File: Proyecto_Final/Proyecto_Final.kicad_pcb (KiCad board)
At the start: 2 copper layers, 68.6 x 53.3 mm, 98 parts, among them J1 Conn_01x10, J10 Conn_01x02, J2 Conn_01x08, J3 USB_OTG, J4 Conn_01x08, J5 Conn_01x06, J6 Conn_01x02, J7 Conn_01x02, J8 Conn_02x03_Odd_Even, J9 Conn_02x03_Odd_Even, Q1 MMBT3904, Q2 MMBT3904, Q3 MMBT3904, Q4 MMBT3904, Q5 MMBT3904, Q6 MMBT3904, SW1 SW_Push, SW2 SW_Push, SW3 SW_Push, SW4 SW_Push, SW5 SW_Push, SW6 SW_Push, U1 TPS61087DSCR, U2 LM1117-3.3, U3 L293D, U4 FT232RL, U5 ATXMEGA32A4U-AU, U6 MODULE-BLUETOOTH-HC-05(34P-27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

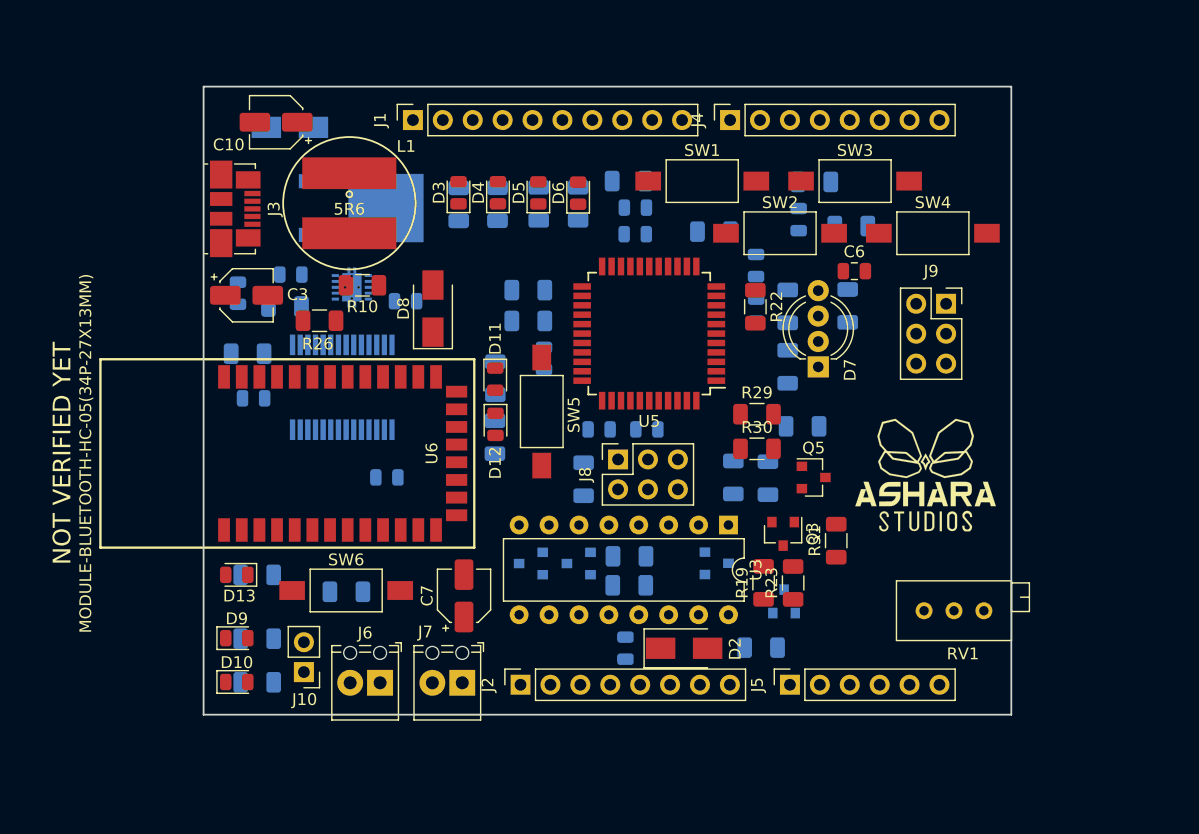
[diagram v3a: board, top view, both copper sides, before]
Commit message: se crean zonas de tierra
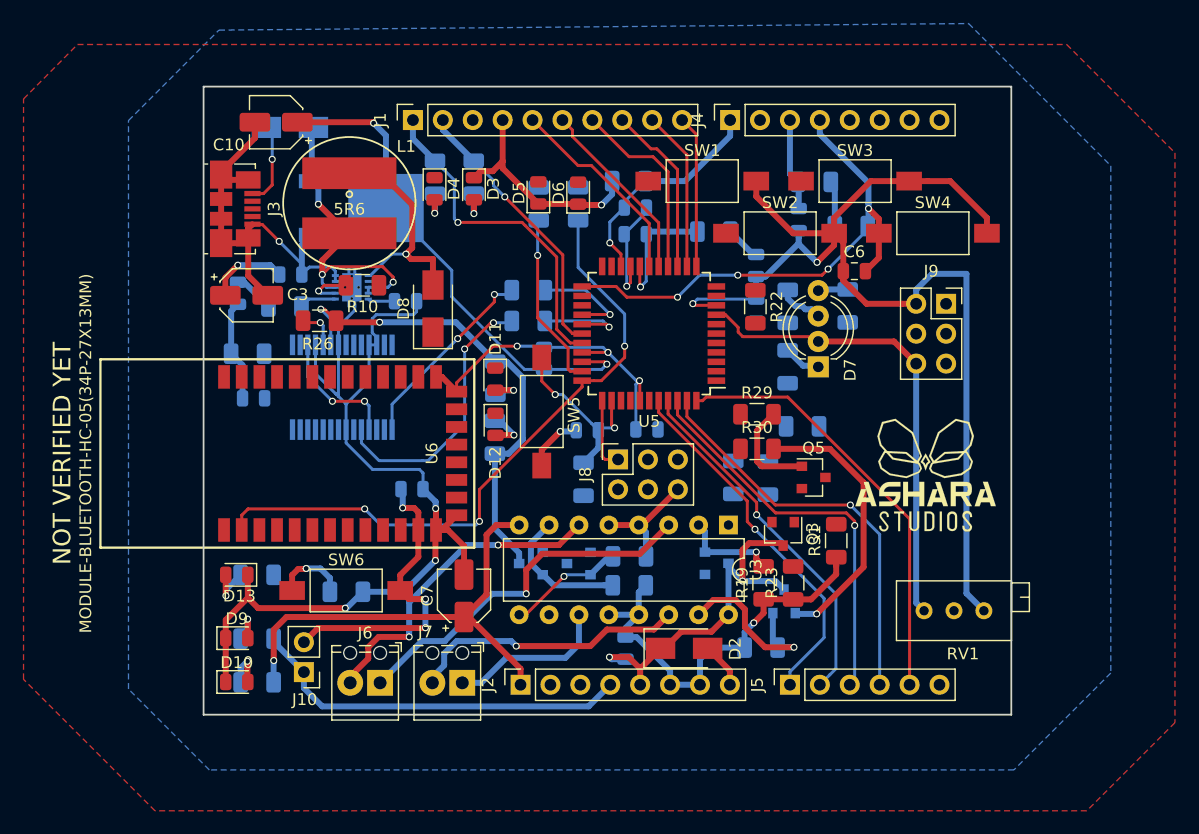
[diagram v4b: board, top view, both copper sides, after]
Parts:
- moved R7 5.78 mm to (141.8, 85.3), turned to 90 degrees
- moved D4 5.40 mm to (141.8, 86.3), turned to 270 degrees
- moved R6 2.63 mm to (145.1, 85.3), turned to 90 degrees
- moved C18 2.35 mm to (139.9, 111.8), turned to 0 degrees
- moved D3 1.36 mm to (145.1, 86.3), turned to 270 degrees
- moved C17 1.00 mm to (154.8, 106.8), turned to 180 degrees
- turned C1 to 180 degrees
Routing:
- net GND: track 0.00 -> 285.8 mm, vias 0 -> 11
- net +3V3: track 0.00 -> 179.0 mm, vias 0 -> 5
- net +5V: track 0.00 -> 106.8 mm, vias 0 -> 8
- net /BT_RX: track 0.00 -> 55.6 mm, vias 0 -> 3
- net /PD3: track 0.00 -> 44.2 mm, vias 0 -> 4
- net +12V: track 0.00 -> 39.9 mm, vias 0 -> 1
- net /A4: track 0.00 -> 36.6 mm
- net /A3: track 0.00 -> 34.6 mm, vias 0 -> 1
- net /A2: track 0.00 -> 34.0 mm, vias 0 -> 1
- net Net-(J6-Pad1): track 0.00 -> 31.3 mm, vias 0 -> 1
- net /A0: track 0.00 -> 31.1 mm, vias 0 -> 1
- net /A1: track 0.00 -> 30.6 mm, vias 0 -> 1
- net /LED2: track 0.00 -> 28.7 mm, vias 0 -> 1
- net Net-(J6-Pad2): track 0.00 -> 27.6 mm, vias 0 -> 2
- net +3.3VP: track 0.00 -> 26.1 mm, vias 0 -> 3
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- added copper zone on B.Cu, net GND
- added copper zone on F.Cu, net GND

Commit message: route manual terminado
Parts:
- moved R10 9.76 mm to (145.3, 93.2), turned to 90 degrees
- moved D4 0.71 mm to (142.5, 86.3)
- moved R7 0.71 mm to (142.5, 85.3)
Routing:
- net GND: track 285.8 -> 371.9 mm, vias 11 -> 22
- net +3V3: track 179.0 -> 245.5 mm, vias 5 -> 13
- net +12V: track 39.9 -> 100.3 mm, vias 1 -> 3
- net /RESET: track 15.7 -> 69.8 mm, vias 2 -> 5
- net +5V: track 106.8 -> 160.7 mm, vias 8 -> 12
- net /SCK: track 17.2 -> 65.8 mm, vias 0 -> 4
- net /BT_STATE: track 12.9 -> 60.3 mm, vias 0 -> 4
- net /TXD1: track 8.07 -> 49.9 mm, vias 1 -> 3
- net /3A: track 0.00 -> 40.7 mm, vias 0 -> 4
- net /PD4: track 0.00 -> 40.3 mm, vias 0 -> 2
- net /PD5: track 0.00 -> 40.0 mm, vias 0 -> 2
- net /RXD1: track 8.78 -> 48.3 mm, vias 1 -> 4
- net /PD2: track 7.82 -> 46.9 mm, vias 0 -> 8
- net /A5: track 0.00 -> 38.3 mm, vias 0 -> 2
- net Net-(Q4-Pad1): track 0.00 -> 36.6 mm, vias 0 -> 1
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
